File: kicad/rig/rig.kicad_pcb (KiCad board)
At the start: 4 copper layers, 160 x 100 mm, 37 parts, among them J1 Baud rate set, J2 TTL-USB, J3 5V DC, SW1 RESET, SW2 POWER, U1 DCJ11, U2 DC319, U3 SN74AHCT14N, U4 74F821SPC, U5 74AHCT541, U6 GAL16V8, Y1 4000 kHz, Y2 614.4 kHz

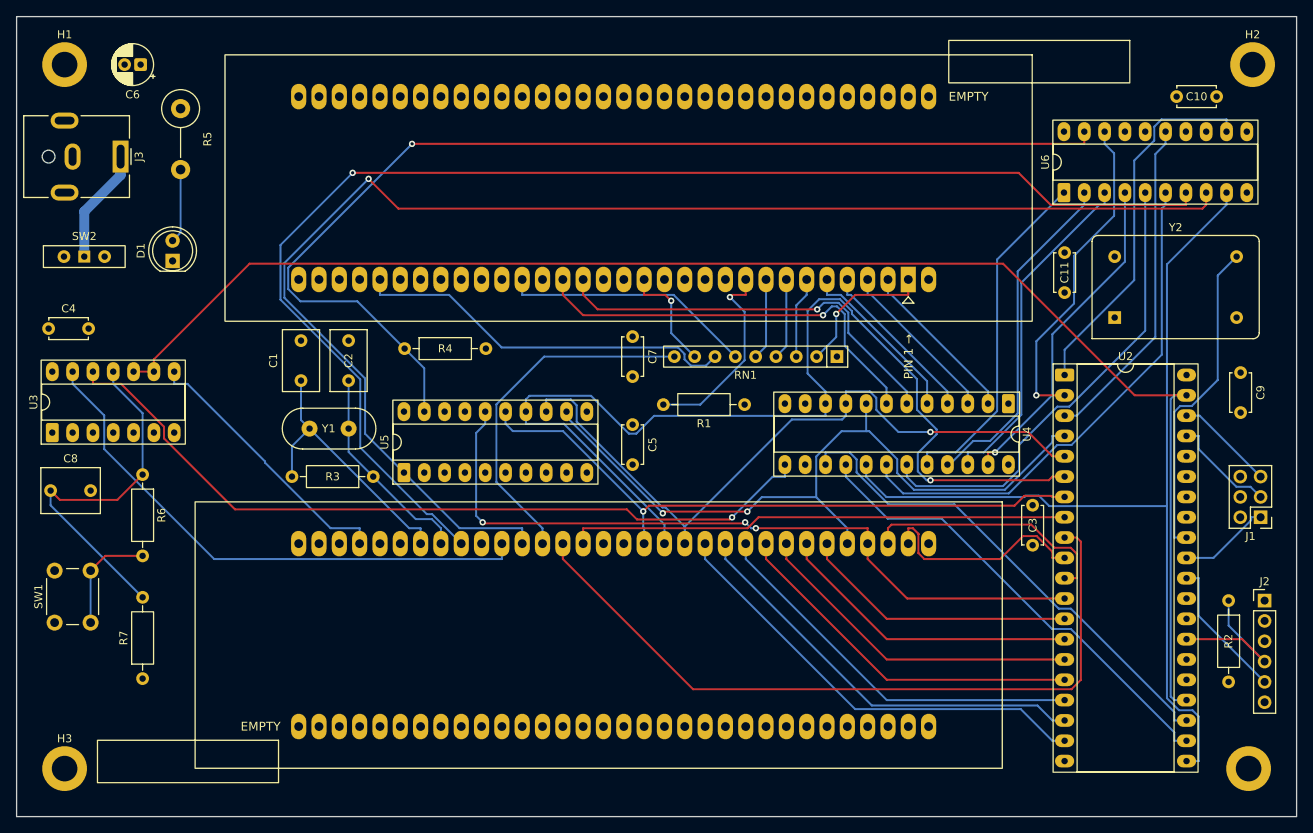
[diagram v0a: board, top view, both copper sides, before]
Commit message: Update KiCad rig for GAL20V8A and late DV capture
Add the GAL20V8A-15LP symbol and complete the matching schematic and routing. Keep separate read and write test points, widen the input power trace to 1.1 mm, and update bypass capacitor placement.

Checked physical pin connectivity, startup bits, current GAL20V8 working-tree logic, and conditional bus timing. PCB DRC and schematic parity pass. Hardware operation remains untested.
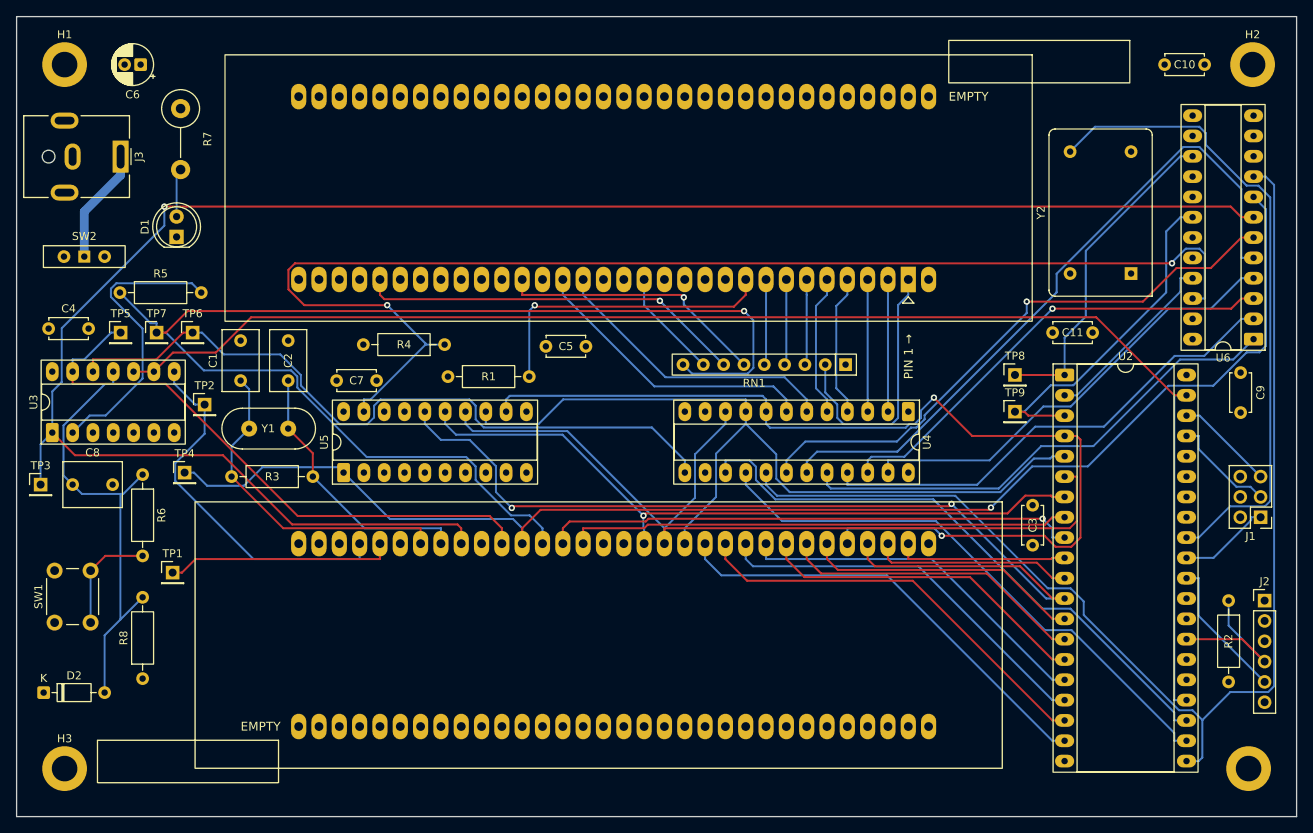
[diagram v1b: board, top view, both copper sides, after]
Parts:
- added D2: 1N4148, Diode_THT:D_DO-35_SOD27_P7.62mm_Horizontal, F.Cu at (58.4, 129.5)
- added R5: 0, Resistor_THT:R_Axial_DIN0207_L6.3mm_D2.5mm_P10.16mm_Horizontal, F.Cu at (67.9, 79.5)
- added TP1: CLK2, Connector_PinHeader_2.54mm:PinHeader_1x01_P2.54mm_Vertical, F.Cu at (74.5, 114.5)
- added TP2: ~{INIT}, Connector_PinHeader_2.54mm:PinHeader_1x01_P2.54mm_Vertical, F.Cu at (78.5, 93.5)
- added TP3: ~{SCTL}, Connector_PinHeader_2.54mm:PinHeader_1x01_P2.54mm_Vertical, F.Cu at (58.0, 103.5)
- added TP4: ~{BUFCTL}, Connector_PinHeader_2.54mm:PinHeader_1x01_P2.54mm_Vertical, F.Cu at (76.0, 102.0)
- added TP5: ~{ALE}, Connector_PinHeader_2.54mm:PinHeader_1x01_P2.54mm_Vertical, F.Cu at (68.0, 84.5)
- added TP6: LE, Connector_PinHeader_2.54mm:PinHeader_1x01_P2.54mm_Vertical, F.Cu at (77.0, 84.5)
- added TP7: DV, Connector_PinHeader_2.54mm:PinHeader_1x01_P2.54mm_Vertical, F.Cu at (72.5, 84.5)
- added TP8: ~{OE}, Connector_PinHeader_2.54mm:PinHeader_1x01_P2.54mm_Vertical, F.Cu at (179.8, 89.8)
- added TP9: ~{WEL}, Connector_PinHeader_2.54mm:PinHeader_1x01_P2.54mm_Vertical, F.Cu at (179.8, 94.4)
- U6: value GAL16V8 -> GAL20V8A-15LP; footprint Package_DIP:DIP-20_W7.62mm_Socket_LongPads -> Package_DIP:DIP-24_W7.62mm_Socket_LongPads
- moved C7 37.4 mm to (95.0, 90.5), turned to 0 degrees
- moved R1 37.2 mm to (108.9, 90.0), turned to 0 degrees
- moved U6 30.0 mm to (209.6, 85.3), turned to 180 degrees
- moved C5 14.6 mm to (121.2, 86.2), turned to 0 degrees
- moved U4 12.5 mm to (166.5, 94.4)
- moved C11 10.1 mm to (184.5, 84.5), turned to 0 degrees
- moved Y1 7.55 mm to (84.1, 96.5)
- moved C1 7.55 mm to (83.0, 90.5)
- moved C2 7.55 mm to (89.0, 90.5)
- moved R3 7.55 mm to (92.0, 102.5)
- moved U5 7.55 mm to (95.9, 102.0)
- moved Y2 5.87 mm to (194.3, 77.1), turned to 90 degrees
- moved R4 5.02 mm to (108.5, 86.0), turned to 180 degrees
- moved C10 4.27 mm to (203.5, 51.0)
- moved D1 3.04 mm to (75.0, 72.5)
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- renumbered R5 to R7, R7 to R8
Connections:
- U1 pad 34: unconnected-(U1-CLK2-Pad34) -> Net-(U1-CLK2)
- U3 pad 1: GND -> /~{SCTL}
- U3 pad 2: unconnected-(U3-Pad2) -> Net-(R5-Pad2)
- U6 pad 11: VCC -> GND
- U6 pad 12: /~{OE} -> GND
- U6 pad 13: unconnected-(U6-F_{1}-Pad13) -> GND
- U6 pad 14: unconnected-(U6-F_{2}-Pad14) -> GND
- U6 pad 15: /~{WEL} -> /~{OE}
- U6 pad 18: /~{IO} -> /~{WEL}
- U6 pad 19: /~{GPREAD} -> unconnected-(U6-I/O4-Pad19)
- U6 pad 20: VCC -> unconnected-(U6-I/O5-Pad20)
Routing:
- net /DV: track 44.5 -> 161.1 mm, vias 0 -> 1
- net /~{SCTL}: track 167.2 -> 235.9 mm
- net /UART_CLK: track 40.7 -> 81.1 mm
- net Net-(R5-Pad2): track 0.00 -> 36.5 mm
- net /A0: track 119.1 -> 152.4 mm
- net /DAL0: track 93.3 -> 126.0 mm
- net Net-(U1-CLK2): track 0.00 -> 28.5 mm
- net /DAL8: track 93.7 -> 121.4 mm, vias 3 -> 2
- net /LBS0: track 59.0 -> 85.6 mm
- net /DAL5: track 93.4 -> 66.8 mm, vias 0 -> 1
- net /~{GPREAD}: track 136.6 -> 160.1 mm, vias 1 -> 2
- net /DAL2: track 133.7 -> 112.4 mm, vias 1 -> 0
- net /LAIO3: track 43.2 -> 62.8 mm
- net /LAIO2: track 42.5 -> 60.9 mm
- net /~{IO}: track 41.0 -> 23.1 mm, vias 1 -> 0
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- added copper zone on In2.Cu, net GND
- added copper zone on In1.Cu, net VCC
- removed copper zone on In1.Cu, net GND
- removed copper zone on In2.Cu, net VCC
